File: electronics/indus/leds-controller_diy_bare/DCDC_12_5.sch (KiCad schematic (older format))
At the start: 6 parts

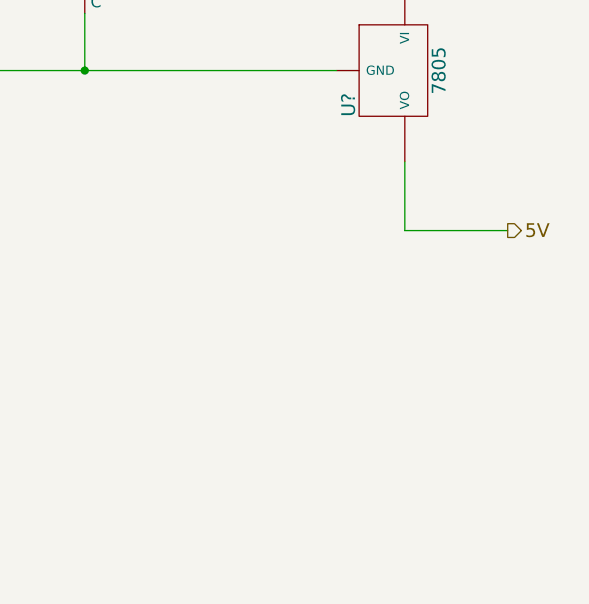
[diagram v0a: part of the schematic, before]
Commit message: schema prctically ok missing refs
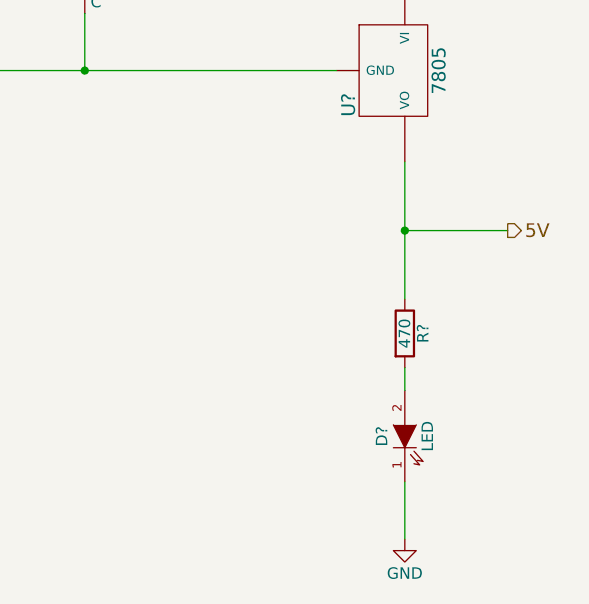
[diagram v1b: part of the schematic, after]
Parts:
- added D?: LED, symbol LED
- added R?: 470, symbol R
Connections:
- net 5V: now also R?.1
- net GND: now also D?.1 (K)
- new net: D?.2 (A), R?.2
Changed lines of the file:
@@
 $Descr A4 11693 8268
 encoding utf-8
-Sheet 9 9
+Sheet 8 9
 Title ""
 Date ""
@@
 $EndComp
 Wire Wire Line
-	9450 4350 9450 4650
+	9450 4350 9450 4950
 Wire Wire Line
 	9450 4650 9900 4650
@@
 	3950 3650 3950 3950
 Connection ~ 5250 3950
+$Comp
+L LED D?
+U 1 1 5764C960
+P 9450 5550
+F 0 "D?" H 9450 5650 50  0000 C CNN
+F 1 "LED" H 9450 5450 50  0000 C CNN
+F 2 "" H 9450 5550 50  0000 C CNN
+F 3 "" H 9450 5550 50  0000 C CNN
+	1    9450 5550
+	0    -1   -1   0
+$EndComp
+$Comp
+L R R?
+U 1 1 5764C967
+P 9450 5100
+F 0 "R?" V 9530 5100 50  0000 C CNN
+F 1 "470" V 9450 5100 50  0000 C CNN
+F 2 "" V 9380 5100 50  0000 C CNN
+F 3 "" H 9450 5100 50  0000 C CNN
+	1    9450 5100
+	1    0    0    -1
+$EndComp
+Wire Wire Line
+	9450 5250 9450 5350
+$Comp
+L GND #PWR?
+U 1 1 5764C97D
+P 9450 6000
+F 0 "#PWR?" H 9450 5750 50  0001 C CNN
+F 1 "GND" H 9450 5850 50  0000 C CNN
+F 2 "" H 9450 6000 50  0000 C CNN
+F 3 "" H 9450 6000 50  0000 C CNN
+	1    9450 6000
+	1    0    0    -1
+$EndComp
+Connection ~ 9450 4650
+Wire Wire Line
+	9450 5750 9450 6000
 $EndSCHEMATC

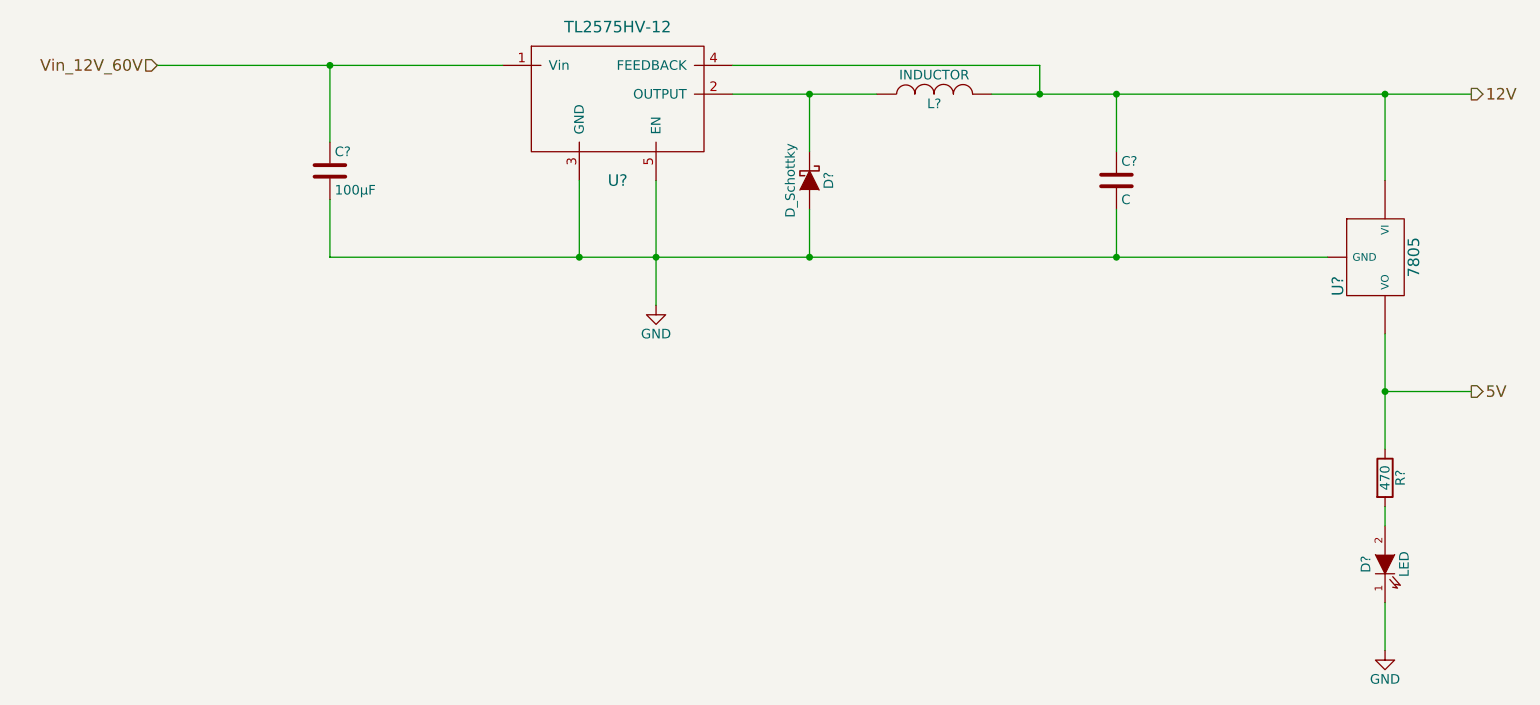
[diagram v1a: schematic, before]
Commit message: schema prctically ok missing refs
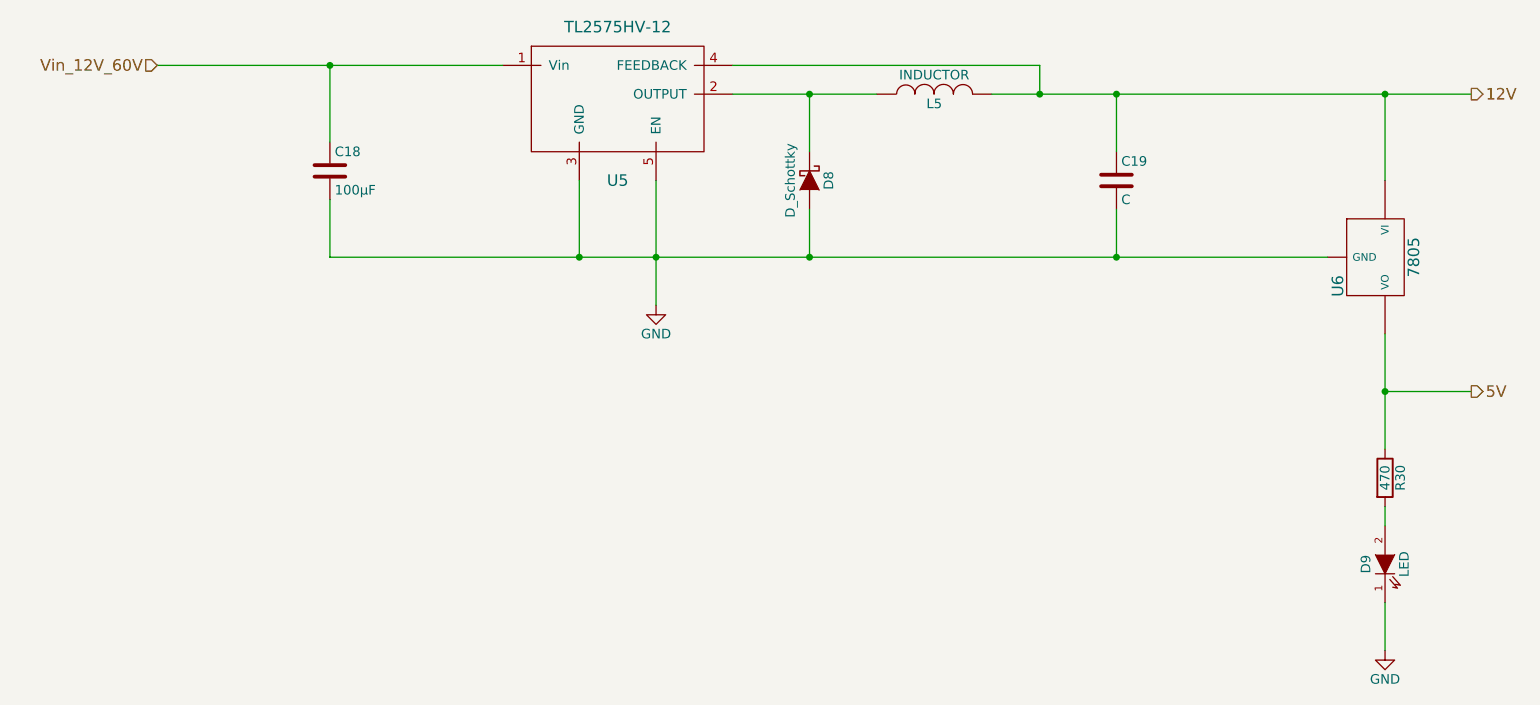
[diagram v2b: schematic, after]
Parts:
- gave numbers to parts that had none: 8
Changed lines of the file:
@@
 $EndDescr
 $Comp
-L TL2575 U?
+L TL2575 U5
 U 1 1 5762406A
 P 5450 3200
-F 0 "U?" H 5450 2850 60  0000 C CNN
+F 0 "U5" H 5450 2850 60  0000 C CNN
 F 1 "TL2575HV-12" H 5450 3650 60  0000 C CNN
 F 2 "" H 5450 3200 60  0000 C CNN
@@
 	3050 2950 4850 2950
 $Comp
-L GND #PWR026
+L GND #PWR17
 U 1 1 576240CC
 P 5650 4200
-F 0 "#PWR026" H 5650 3950 50  0001 C CNN
+F 0 "#PWR17" H 5650 3950 50  0001 C CNN
 F 1 "GND" H 5650 4050 50  0000 C CNN
 F 2 "" H 5650 4200 50  0000 C CNN
@@
 Connection ~ 5650 3950
 $Comp
-L D_Schottky D?
+L D_Schottky D8
 U 1 1 576240F0
 P 6450 3550
-F 0 "D?" H 6450 3650 50  0000 C CNN
+F 0 "D8" H 6450 3650 50  0000 C CNN
 F 1 "D_Schottky" H 6450 3450 50  0000 C CNN
 F 2 "" H 6450 3550 50  0000 C CNN
@@
 	6050 3100 6800 3100
 $Comp
-L INDUCTOR L?
+L INDUCTOR L5
 U 1 1 57624177
 P 7100 3100
-F 0 "L?" V 7050 3100 50  0000 C CNN
+F 0 "L5" V 7050 3100 50  0000 C CNN
 F 1 "INDUCTOR" V 7200 3100 50  0000 C CNN
 F 2 "" H 7100 3100 50  0000 C CNN
@@
 	6450 3400 6450 3100
 $Comp
-L C C?
+L C C19
 U 1 1 57624207
 P 8050 3550
-F 0 "C?" H 8075 3650 50  0000 L CNN
+F 0 "C19" H 8075 3650 50  0000 L CNN
 F 1 "C" H 8075 3450 50  0000 L CNN
 F 2 "" H 8088 3400 50  0000 C CNN
@@
 Connection ~ 6450 3950
 $Comp
-L 7805 U?
+L 7805 U6
 U 1 1 576245A9
 P 9400 3950
-F 0 "U?" H 9550 3754 60  0000 C CNN
+F 0 "U6" H 9550 3754 60  0000 C CNN
 F 1 "7805" H 9400 4150 60  0000 C CNN
 F 2 "" H 9400 3950 60  0000 C CNN
@@
 12V
 $Comp
-L C C?
+L C C18
 U 1 1 5762464E
 P 3950 3500
-F 0 "C?" H 3975 3600 50  0000 L CNN
+F 0 "C18" H 3975 3600 50  0000 L CNN
 F 1 "100µF" H 3975 3400 50  0000 L CNN
 F 2 "" H 3988 3350 50  0000 C CNN
@@
 Connection ~ 5250 3950
 $Comp
-L LED D?
+L LED D9
 U 1 1 5764C960
 P 9450 5550
-F 0 "D?" H 9450 5650 50  0000 C CNN
+F 0 "D9" H 9450 5650 50  0000 C CNN
 F 1 "LED" H 9450 5450 50  0000 C CNN
 F 2 "" H 9450 5550 50  0000 C CNN
@@
 $EndComp
 $Comp
-L R R?
+L R R30
 U 1 1 5764C967
 P 9450 5100
-F 0 "R?" V 9530 5100 50  0000 C CNN
+F 0 "R30" V 9530 5100 50  0000 C CNN
 F 1 "470" V 9450 5100 50  0000 C CNN
 F 2 "" V 9380 5100 50  0000 C CNN
@@
 	9450 5250 9450 5350
 $Comp
-L GND #PWR?
+L GND #PWR18
 U 1 1 5764C97D
 P 9450 6000
-F 0 "#PWR?" H 9450 5750 50  0001 C CNN
+F 0 "#PWR18" H 9450 5750 50  0001 C CNN
 F 1 "GND" H 9450 5850 50  0000 C CNN
 F 2 "" H 9450 6000 50  0000 C CNN

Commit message: bom refs etc
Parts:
- C19: value C -> 330µF LOW ESR 35V - EEEFC1V331P
- D8: value D_Schottky -> CD214A-B160LF
- D9: value LED -> KP-2012SGC
- L5: value INDUCTOR -> SRR1210A-681M
- U6: value 7805 -> L7805AD2T-TR
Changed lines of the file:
@@
 P 6450 3550
 F 0 "D8" H 6450 3650 50  0000 C CNN
-F 1 "D_Schottky" H 6450 3450 50  0000 C CNN
+F 1 "CD214A-B160LF" H 6450 3450 50  0000 C CNN
 F 2 "" H 6450 3550 50  0000 C CNN
 F 3 "" H 6450 3550 50  0000 C CNN
@@
 P 7100 3100
 F 0 "L5" V 7050 3100 50  0000 C CNN
-F 1 "INDUCTOR" V 7200 3100 50  0000 C CNN
+F 1 "SRR1210A-681M" V 7200 3100 50  0000 C CNN
 F 2 "" H 7100 3100 50  0000 C CNN
 F 3 "" H 7100 3100 50  0000 C CNN
@@
 P 8050 3550
 F 0 "C19" H 8075 3650 50  0000 L CNN
-F 1 "C" H 8075 3450 50  0000 L CNN
+F 1 "330µF LOW ESR 35V - EEEFC1V331P" H 7350 3400 50  0000 L CNN
 F 2 "" H 8088 3400 50  0000 C CNN
 F 3 "" H 8050 3550 50  0000 C CNN
@@
 P 9400 3950
 F 0 "U6" H 9550 3754 60  0000 C CNN
-F 1 "7805" H 9400 4150 60  0000 C CNN
+F 1 "L7805AD2T-TR" H 9400 4150 60  0000 C CNN
 F 2 "" H 9400 3950 60  0000 C CNN
 F 3 "" H 9400 3950 60  0000 C CNN
@@
 P 9450 5550
 F 0 "D9" H 9450 5650 50  0000 C CNN
-F 1 "LED" H 9450 5450 50  0000 C CNN
+F 1 "KP-2012SGC" H 9450 5450 50  0000 C CNN
 F 2 "" H 9450 5550 50  0000 C CNN
 F 3 "" H 9450 5550 50  0000 C CNN

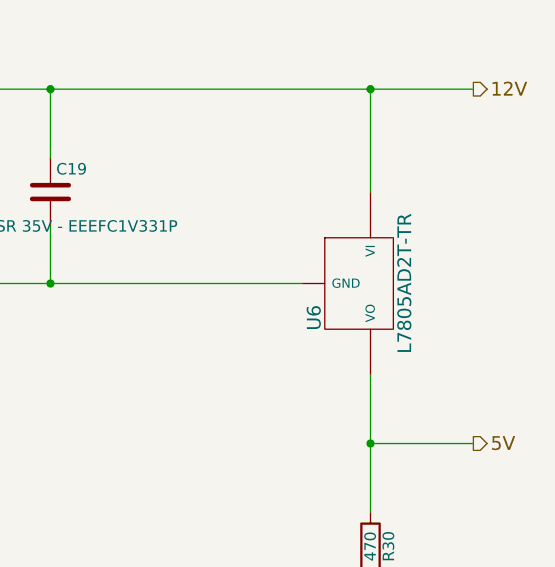
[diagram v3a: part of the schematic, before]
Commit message: footprint with libraries
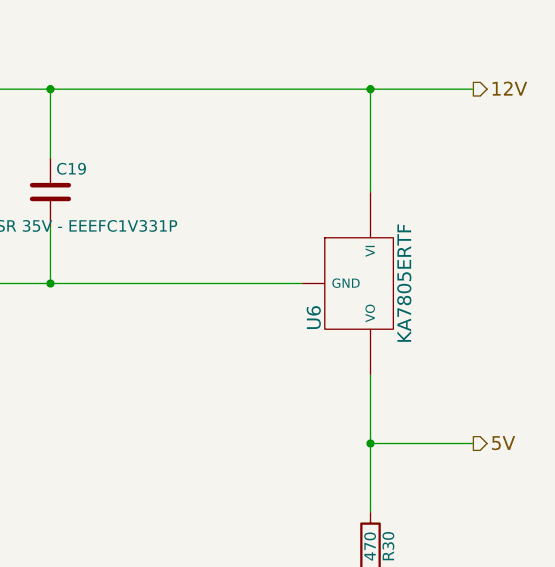
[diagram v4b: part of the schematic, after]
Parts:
- C18: footprint (none) -> Capacitors_ThroughHole:C_Radial_D10_L20_P5
- C19: footprint (none) -> risebox:CAPA_EEEFC1V331P
- D8: footprint (none) -> ab2_passive:AB2_DO-214AC
- D9: footprint (none) -> risebox:LED-KPH-2012SGC
- L5: footprint (none) -> risebox:INDUC_SRR1210A
- R30: footprint (none) -> Resistors_SMD:R_0805
- U5: footprint (none) -> TO_SOT_Packages_SMD:TO-263-5Lead
- U6: value L7805AD2T-TR -> KA7805ERTF; footprint (none) -> risebox:KA7805ERTF_TO-252-3
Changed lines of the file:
@@
 F 0 "U5" H 5450 2850 60  0000 C CNN
 F 1 "TL2575HV-12" H 5450 3650 60  0000 C CNN
-F 2 "" H 5450 3200 60  0000 C CNN
+F 2 "TO_SOT_Packages_SMD:TO-263-5Lead" H 5450 3200 60  0001 C CNN
 F 3 "" H 5450 3200 60  0000 C CNN
 	1    5450 3200
@@
 	3050 2950 4850 2950
 $Comp
-L GND #PWR17
+L GND #PWR018
 U 1 1 576240CC
 P 5650 4200
-F 0 "#PWR17" H 5650 3950 50  0001 C CNN
+F 0 "#PWR018" H 5650 3950 50  0001 C CNN
 F 1 "GND" H 5650 4050 50  0000 C CNN
 F 2 "" H 5650 4200 50  0000 C CNN
@@
 F 0 "D8" H 6450 3650 50  0000 C CNN
 F 1 "CD214A-B160LF" H 6450 3450 50  0000 C CNN
-F 2 "" H 6450 3550 50  0000 C CNN
+F 2 "ab2_passive:AB2_DO-214AC" H 6450 3550 50  0001 C CNN
 F 3 "" H 6450 3550 50  0000 C CNN
 	1    6450 3550
@@
 F 0 "L5" V 7050 3100 50  0000 C CNN
 F 1 "SRR1210A-681M" V 7200 3100 50  0000 C CNN
-F 2 "" H 7100 3100 50  0000 C CNN
+F 2 "risebox:INDUC_SRR1210A" H 7100 3100 50  0001 C CNN
 F 3 "" H 7100 3100 50  0000 C CNN
 	1    7100 3100
@@
 F 0 "C19" H 8075 3650 50  0000 L CNN
 F 1 "330µF LOW ESR 35V - EEEFC1V331P" H 7350 3400 50  0000 L CNN
-F 2 "" H 8088 3400 50  0000 C CNN
+F 2 "risebox:CAPA_EEEFC1V331P" H 8088 3400 50  0001 C CNN
 F 3 "" H 8050 3550 50  0000 C CNN
 	1    8050 3550
@@
 P 9400 3950
 F 0 "U6" H 9550 3754 60  0000 C CNN
-F 1 "L7805AD2T-TR" H 9400 4150 60  0000 C CNN
-F 2 "" H 9400 3950 60  0000 C CNN
+F 1 "KA7805ERTF" H 9400 4150 60  0000 C CNN
+F 2 "risebox:KA7805ERTF_TO-252-3" H 9400 3950 60  0001 C CNN
 F 3 "" H 9400 3950 60  0000 C CNN
 	1    9400 3950
@@
 F 0 "C18" H 3975 3600 50  0000 L CNN
 F 1 "100µF" H 3975 3400 50  0000 L CNN
-F 2 "" H 3988 3350 50  0000 C CNN
+F 2 "Capacitors_ThroughHole:C_Radial_D10_L20_P5" H 3988 3350 50  0001 C CNN
 F 3 "" H 3950 3500 50  0000 C CNN
 	1    3950 3500
@@
 F 0 "D9" H 9450 5650 50  0000 C CNN
 F 1 "KP-2012SGC" H 9450 5450 50  0000 C CNN
-F 2 "" H 9450 5550 50  0000 C CNN
+F 2 "risebox:LED-KPH-2012SGC" H 9450 5550 50  0001 C CNN
 F 3 "" H 9450 5550 50  0000 C CNN
 	1    9450 5550
@@
 F 0 "R30" V 9530 5100 50  0000 C CNN
 F 1 "470" V 9450 5100 50  0000 C CNN
-F 2 "" V 9380 5100 50  0000 C CNN
+F 2 "Resistors_SMD:R_0805" V 9380 5100 50  0001 C CNN
 F 3 "" H 9450 5100 50  0000 C CNN
 	1    9450 5100
@@
 	9450 5250 9450 5350
 $Comp
-L GND #PWR18
+L GND #PWR019
 U 1 1 5764C97D
 P 9450 6000
-F 0 "#PWR18" H 9450 5750 50  0001 C CNN
+F 0 "#PWR019" H 9450 5750 50  0001 C CNN
 F 1 "GND" H 9450 5850 50  0000 C CNN
 F 2 "" H 9450 6000 50  0000 C CNN

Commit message: before routing - no more errors
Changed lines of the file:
@@
 LIBS:contrib
 LIBS:valves
+LIBS:tps54335a
 LIBS:risebox
-LIBS:tps54335a
 LIBS:leds-controller-cache
 EELAYER 25 0
@@
 	3050 2950 4850 2950
 $Comp
-L GND #PWR018
+L GND #PWR017
 U 1 1 576240CC
 P 5650 4200
-F 0 "#PWR018" H 5650 3950 50  0001 C CNN
+F 0 "#PWR017" H 5650 3950 50  0001 C CNN
 F 1 "GND" H 5650 4050 50  0000 C CNN
 F 2 "" H 5650 4200 50  0000 C CNN
@@
 	8050 3950 8050 3700
 Connection ~ 6450 3950
-$Comp
-L 7805 U6
-U 1 1 576245A9
-P 9400 3950
-F 0 "U6" H 9550 3754 60  0000 C CNN
-F 1 "KA7805ERTF" H 9400 4150 60  0000 C CNN
-F 2 "risebox:KA7805ERTF_TO-252-3" H 9400 3950 60  0001 C CNN
-F 3 "" H 9400 3950 60  0000 C CNN
-	1    9400 3950
-	0    1    1    0
-$EndComp
 Wire Wire Line
 	9450 4350 9450 4950
@@
 	9450 5250 9450 5350
 $Comp
-L GND #PWR019
+L GND #PWR018
 U 1 1 5764C97D
 P 9450 6000
-F 0 "#PWR019" H 9450 5750 50  0001 C CNN
+F 0 "#PWR018" H 9450 5750 50  0001 C CNN
 F 1 "GND" H 9450 5850 50  0000 C CNN
 F 2 "" H 9450 6000 50  0000 C CNN
@@
 Wire Wire Line
 	5250 3550 5250 3950
+$Comp
+L 7805 U6
+U 1 1 576F3794
+P 9400 3950
+F 0 "U6" H 9550 3754 50  0000 C CNN
+F 1 "KA7805ERTF" H 9400 4150 50  0000 C CNN
+F 2 "risebox:KA7805ERTF_TO-252-3" H 9400 3950 50  0001 C CNN
+F 3 "" H 9400 3950 50  0000 C CNN
+	1    9400 3950
+	0    1    1    0
+$EndComp
 $EndSCHEMATC
